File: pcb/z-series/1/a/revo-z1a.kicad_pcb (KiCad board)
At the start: 2 copper layers, 198.1 x 16.5 mm, 1 part

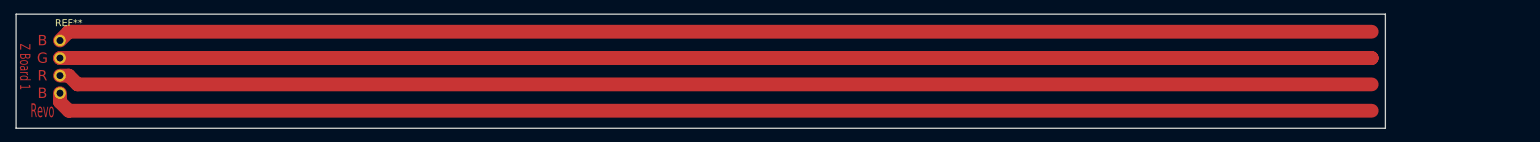
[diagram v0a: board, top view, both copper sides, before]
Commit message: Reorganised the directory structure for PCBs and renamed the Revo Z Board 1 to Revo Z1A
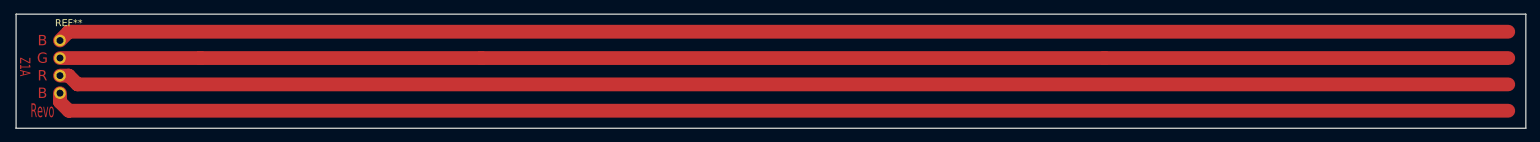
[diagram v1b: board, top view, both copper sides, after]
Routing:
- net (no net): track 951.8 -> 841.0 mm
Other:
- board size 198.1 x 16.5 mm -> 218.4 x 16.5 mm
- board text added: "Z1A"
- board text removed: "Z Board 1"
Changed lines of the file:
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@@
     (thickness 1.6)
     (drawings 10)
-    (tracks 10)
+    (tracks 12)
     (zones 0)
     (modules 1)
@@
   (page User 240.005 101.6)
   (title_block
-    (title "Revo Z Board 1")
-    (date 2020-11-06)
-    (rev 1)
+    (title "Revo Z1A")
+    (date 2020-11-07)
+    (rev 2)
   )
   (layers
@@
     )
   )
-  (gr_text "Z Board 1" (at 22.86 33.02 -90) (layer F.Cu)
+  (gr_text Z1A (at 22.86 33.02 -90) (layer F.Cu)
     (effects (font (size 1.5 1) (thickness 0.25)))
   )
@@
     (effects (font (size 1.5 1.5) (thickness 0.375)))
   )
-  (gr_line (start 219.71 25.4) (end 219.71 41.91) (layer Edge.Cuts) (width 0.1))
-  (gr_line (start 21.59 25.4) (end 219.71 25.4) (layer Edge.Cuts) (width 0.1))
+  (gr_line (start 240.03 25.4) (end 240.03 41.91) (layer Edge.Cuts) (width 0.1))
+  (gr_line (start 21.59 25.4) (end 240.03 25.4) (layer Edge.Cuts) (width 0.1))
   (gr_line (start 21.59 41.91) (end 21.59 25.4) (layer Edge.Cuts) (width 0.1))
-  (gr_line (start 219.71 41.91) (end 21.59 41.91) (layer Edge.Cuts) (width 0.1))
-  (segment (start 29.21 27.94) (end 217.73 27.94) (width 2) (layer F.Cu) (net 0))
-  (segment (start 29.21 39.37) (end 217.73 39.37) (width 2) (layer F.Cu) (net 0))
-  (segment (start 30.48 35.56) (end 217.73 35.56) (width 2) (layer F.Cu) (net 0))
-  (segment (start 27.94 31.75) (end 217.73 31.75) (width 2) (layer F.Cu) (net 0))
-  (segment (start 27.94 31.75) (end 217.73 31.75) (width 2) (layer F.Cu) (net 0))
+  (gr_line (start 240.03 41.91) (end 21.59 41.91) (layer Edge.Cuts) (width 0.1))
   (segment (start 29.21 27.94) (end 27.94 29.21) (width 2) (layer F.Cu) (net 0))
   (segment (start 30.48 35.56) (end 29.21 34.29) (width 2) (layer F.Cu) (net 0))
@@
   (segment (start 29.21 39.37) (end 27.94 38.1) (width 2) (layer F.Cu) (net 0))
   (segment (start 27.94 38.1) (end 27.94 36.83) (width 2) (layer F.Cu) (net 0))
+  (segment (start 29.21 27.94) (end 237.49 27.94) (width 2) (layer F.Cu) (net 0))
+  (segment (start 27.94 31.75) (end 48.26 31.75) (width 2) (layer F.Cu) (net 0))
+  (segment (start 48.26 31.75) (end 88.9 31.75) (width 2) (layer F.Cu) (net 0))
+  (segment (start 88.9 31.75) (end 179.07 31.75) (width 2) (layer F.Cu) (net 0))
+  (segment (start 179.07 31.75) (end 237.49 31.75) (width 2) (layer F.Cu) (net 0))
+  (segment (start 30.48 35.56) (end 237.49 35.56) (width 2) (layer F.Cu) (net 0))
+  (segment (start 29.21 39.37) (end 237.49 39.37) (width 2) (layer F.Cu) (net 0))
 )
